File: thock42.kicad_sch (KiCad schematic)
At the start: 45 parts, among them J1 OLED-128x32, SW1 SW_PUSH, SW10 SW_PUSH, SW11 SW_PUSH, SW12 SW_PUSH, SW13 SW_PUSH, SW14 SW_PUSH, SW15 SW_PUSH, SW16 SW_PUSH, SW17 SW_PUSH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

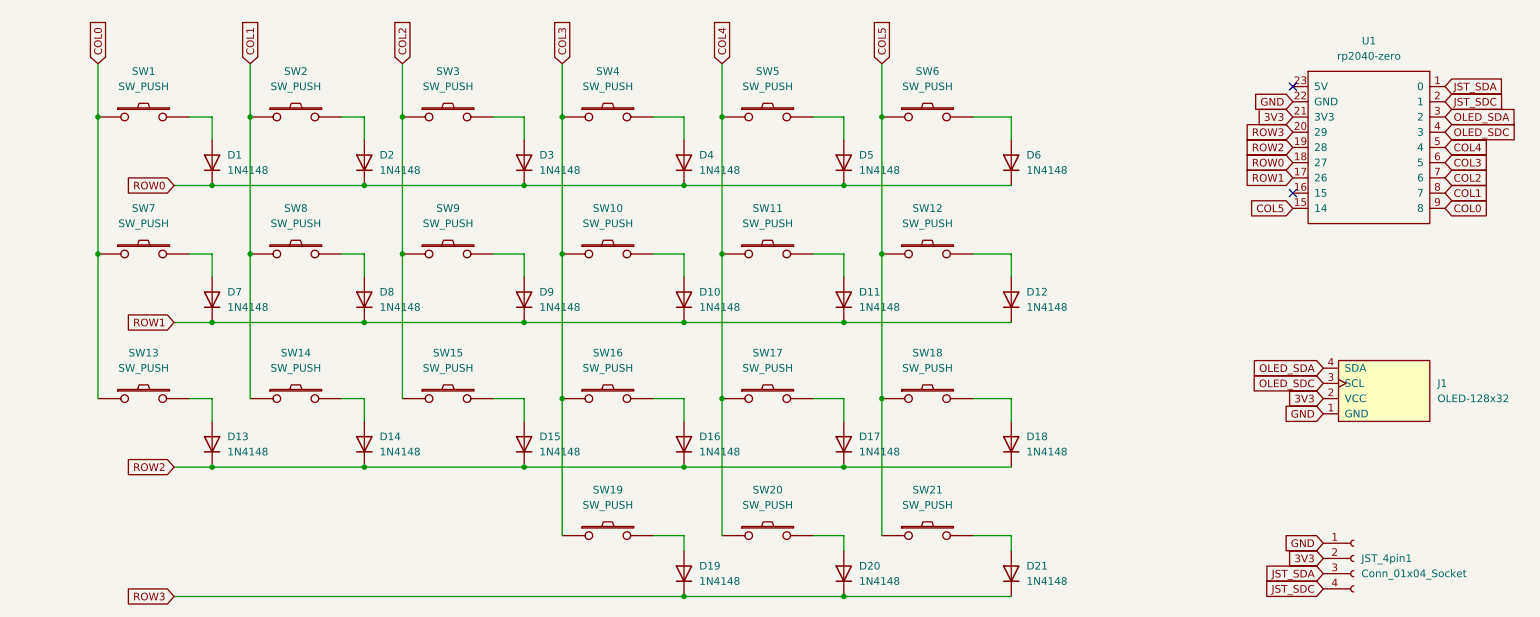
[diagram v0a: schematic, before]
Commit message: 4pin jst with i2c changed to 3pin jst with serial
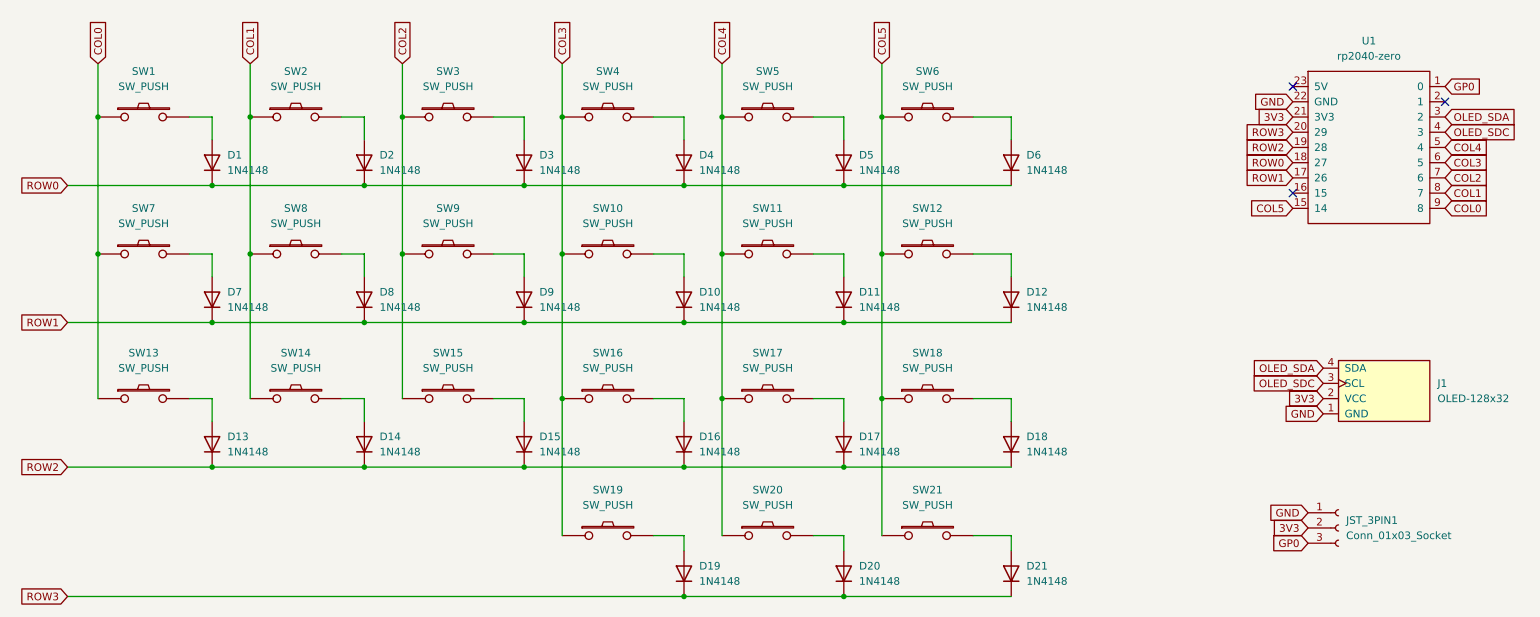
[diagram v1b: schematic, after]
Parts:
- removed JST_4pin1: Conn_01x04_Socket, Connector_JST:JST_XH_S4B-XH-A_1x04_P2.50mm_Horizontal, symbol Connector:Conn_01x04_Socket
- added JST_3PIN1: Conn_01x03_Socket, Connector_JST:JST_XH_S3B-XH-A_1x03_P2.50mm_Horizontal, symbol Connector:Conn_01x03_Socket
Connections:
- net 3V3: now also JST_3PIN1.2 (Pin_2)
- net GND: now also JST_3PIN1.1 (Pin_1)
- net JST_SDA renamed GP0
- net GP0: now also JST_3PIN1.3 (Pin_3)
- net JST_SDC: no longer names the net of U1.2 (1)
- no-connect marks 2 -> 3

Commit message: feat: add switch id silkscreen
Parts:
- SW1, SW10, SW11, SW12, SW13, SW14, SW15, SW16, SW17, SW18, SW19, SW2, SW20, SW21, SW3, SW4, SW5, SW6, SW7, SW8, SW9: footprint pg1350:pg1350-RH -> pg1350:pg1350-RH_silkscreen
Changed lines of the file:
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@@
 			)
 		)
-		(property "Footprint" "pg1350:pg1350-RH"
+		(property "Footprint" "pg1350:pg1350-RH_silkscreen"
 			(at 144.78 58.42 0)
 			(effects
@@
 			)
 		)
-		(property "Footprint" "pg1350:pg1350-RH"
+		(property "Footprint" "pg1350:pg1350-RH_silkscreen"
 			(at 66.04 81.28 0)
 			(effects
@@
 			)
 		)
-		(property "Footprint" "pg1350:pg1350-RH"
+		(property "Footprint" "pg1350:pg1350-RH_silkscreen"
 			(at 118.11 81.28 0)
 			(effects
@@
 			)
 		)
-		(property "Footprint" "pg1350:pg1350-RH"
+		(property "Footprint" "pg1350:pg1350-RH_silkscreen"
 			(at 171.45 81.28 0)
 			(effects
@@
 			)
 		)
-		(property "Footprint" "pg1350:pg1350-RH"
+		(property "Footprint" "pg1350:pg1350-RH_silkscreen"
 			(at 171.45 105.41 0)
 			(effects
@@
 			)
 		)
-		(property "Footprint" "pg1350:pg1350-RH"
+		(property "Footprint" "pg1350:pg1350-RH_silkscreen"
 			(at 118.11 105.41 0)
 			(effects
@@
 			)
 		)
-		(property "Footprint" "pg1350:pg1350-RH"
+		(property "Footprint" "pg1350:pg1350-RH_silkscreen"
 			(at 118.11 58.42 0)
 			(effects
@@
 			)
 		)
-		(property "Footprint" "pg1350:pg1350-RH"
+		(property "Footprint" "pg1350:pg1350-RH_silkscreen"
 			(at 171.45 128.27 0)
 			(effects
@@
 			)
 		)
-		(property "Footprint" "pg1350:pg1350-RH"
+		(property "Footprint" "pg1350:pg1350-RH_silkscreen"
 			(at 144.78 81.28 0)
 			(effects
@@
 			)
 		)
-		(property "Footprint" "pg1350:pg1350-RH"
+		(property "Footprint" "pg1350:pg1350-RH_silkscreen"
 			(at 118.11 128.27 0)
 			(effects
@@
 			)
 		)
-		(property "Footprint" "pg1350:pg1350-RH"
+		(property "Footprint" "pg1350:pg1350-RH_silkscreen"
 			(at 144.78 128.27 0)
 			(effects
@@
 			)
 		)
-		(property "Footprint" "pg1350:pg1350-RH"
+		(property "Footprint" "pg1350:pg1350-RH_silkscreen"
 			(at 91.44 58.42 0)
 			(effects
@@
 			)
 		)
-		(property "Footprint" "pg1350:pg1350-RH"
+		(property "Footprint" "pg1350:pg1350-RH_silkscreen"
 			(at 91.44 105.41 0)
 			(effects
@@
 			)
 		)
-		(property "Footprint" "pg1350:pg1350-RH"
+		(property "Footprint" "pg1350:pg1350-RH_silkscreen"
 			(at 40.64 105.41 0)
 			(effects
@@
 			)
 		)
-		(property "Footprint" "pg1350:pg1350-RH"
+		(property "Footprint" "pg1350:pg1350-RH_silkscreen"
 			(at 66.04 58.42 0)
 			(effects
@@
 			)
 		)
-		(property "Footprint" "pg1350:pg1350-RH"
+		(property "Footprint" "pg1350:pg1350-RH_silkscreen"
 			(at 66.04 105.41 0)
 			(effects
@@
 			)
 		)
-		(property "Footprint" "pg1350:pg1350-RH"
+		(property "Footprint" "pg1350:pg1350-RH_silkscreen"
 			(at 171.45 58.42 0)
 			(effects
@@
 			)
 		)
-		(property "Footprint" "pg1350:pg1350-RH"
+		(property "Footprint" "pg1350:pg1350-RH_silkscreen"
 			(at 91.44 81.28 0)
 			(effects
@@
 			)
 		)
-		(property "Footprint" "pg1350:pg1350-RH"
+		(property "Footprint" "pg1350:pg1350-RH_silkscreen"
 			(at 40.64 58.42 0)
 			(effects
@@
 			)
 		)
-		(property "Footprint" "pg1350:pg1350-RH"
+		(property "Footprint" "pg1350:pg1350-RH_silkscreen"
 			(at 144.78 105.41 0)
 			(effects
@@
 			)
 		)
-		(property "Footprint" "pg1350:pg1350-RH"
+		(property "Footprint" "pg1350:pg1350-RH_silkscreen"
 			(at 40.64 81.28 0)
 			(effects

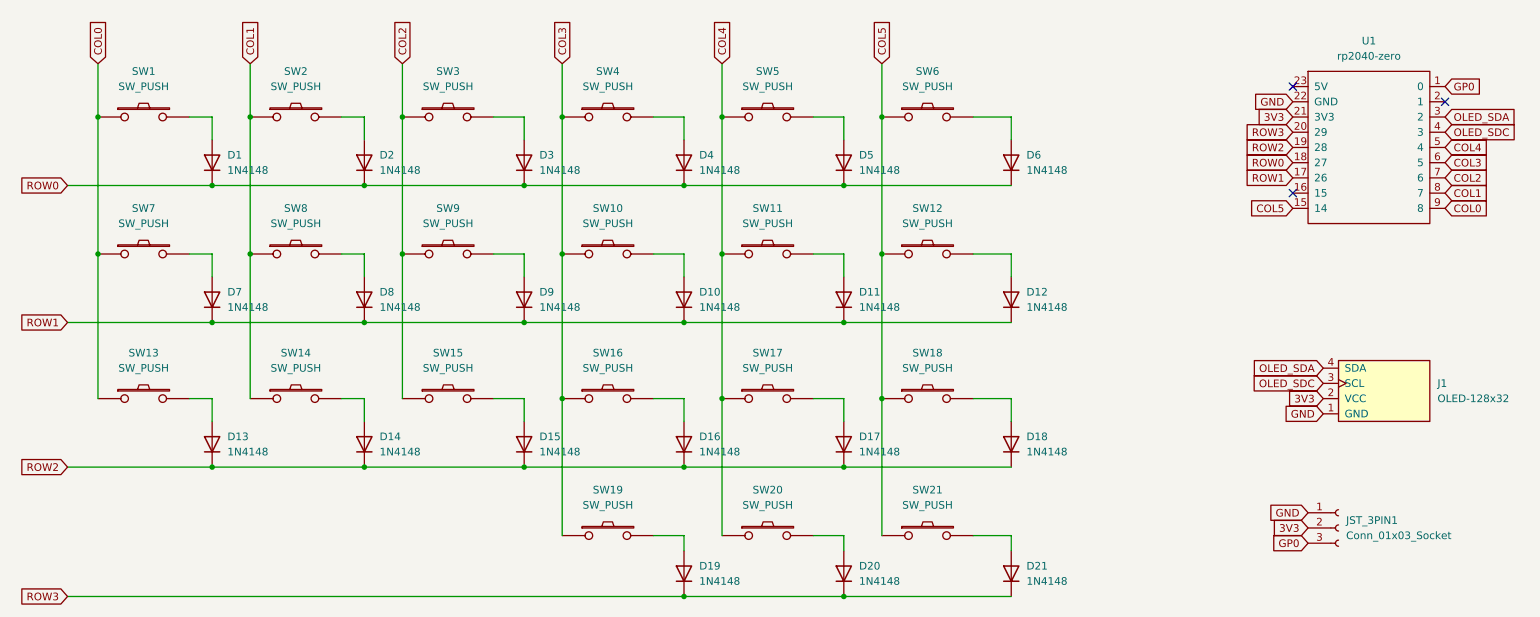
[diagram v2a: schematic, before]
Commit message: update links to libs, jst footprint, and add add mounting hole
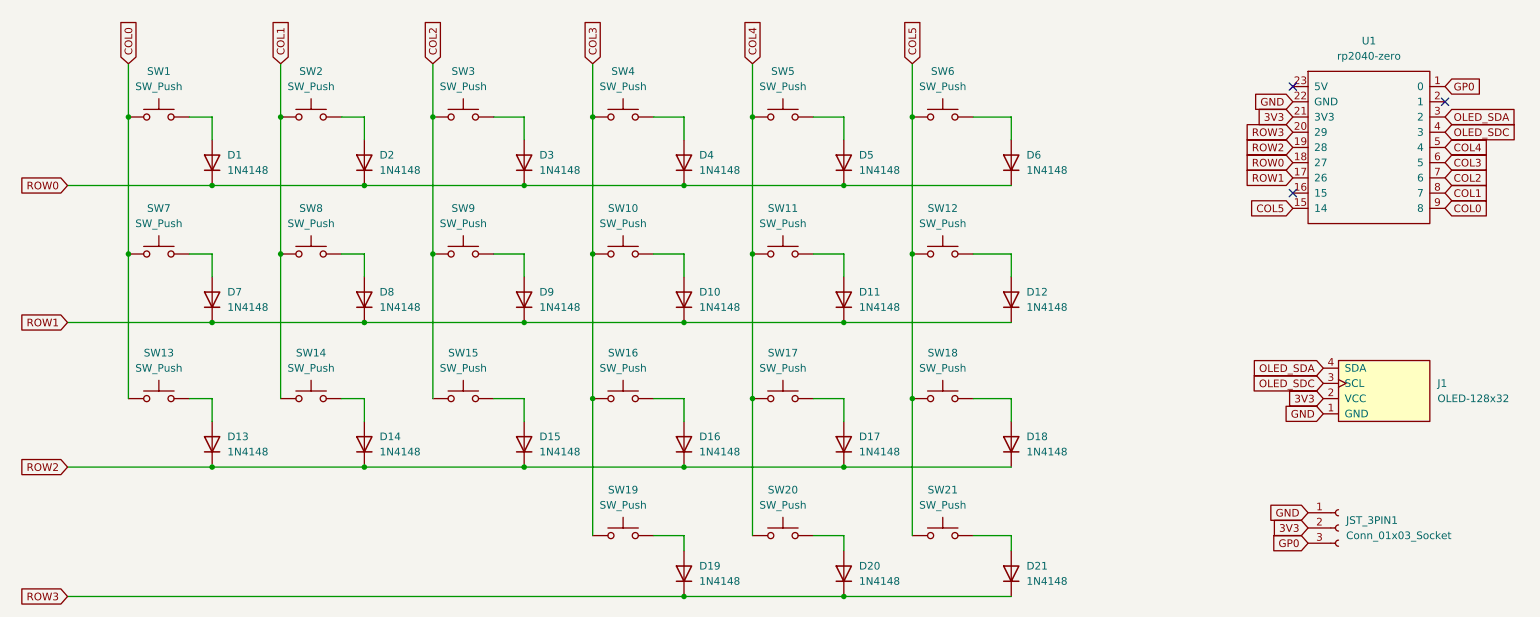
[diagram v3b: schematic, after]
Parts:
- removed SW1, SW10, SW11, SW12, SW13, SW14, SW15, SW16, SW17, SW18, SW19, SW2, SW20, SW21, SW3, SW4, SW5, SW6, SW7, SW8, SW9: SW_PUSH, pg1350:pg1350-RH_silkscreen, symbol kbd:SW_PUSH
- added SW1, SW10, SW11, SW12, SW13, SW14, SW15, SW16, SW17, SW18, SW19, SW2, SW20, SW21, SW3, SW4, SW5, SW6, SW7, SW8, SW9: SW_Push, thock42:pg1350-RH_silkscreen, symbol Switch:SW_Push
- J1: footprint display_kleeb:OLED-128x32-double-sided -> thock42:OLED-128x32-double-sided; symbol display_kleeb:OLED-128x32 -> thock42:OLED-128x32
- JST_3PIN1: footprint Connector_JST:JST_XH_S3B-XH-A_1x03_P2.50mm_Horizontal -> Connector_JST:JST_PH_S3B-PH-K_1x03_P2.00mm_Horizontal
- U1: footprint mcu_kleeb:rp2040-zero-tht_nobtm_reversible -> thock42:rp2040-zero-tht_nobtm_reversible; symbol mcu_kleeb:rp2040-zero -> thock42:rp2040-zero_nobtm
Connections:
- net COL0: now also SW1.1, SW13.1, SW7.1
- net COL1: now also SW14.1, SW2.1, SW8.1
- net COL2: now also SW15.1, SW3.1, SW9.1
- net COL3: now also SW10.1, SW16.1, SW19.1, SW4.1
- net COL4: now also SW11.1, SW17.1, SW20.1, SW5.1
- net COL5: now also SW12.1, SW18.1, SW21.1, SW6.1
- net at D5.2 (A): now also SW5.2
- net at D17.2 (A): now also SW17.2
- net at D8.2 (A): now also SW8.2
- net at D10.2 (A): now also SW10.2
- net at D12.2 (A): now also SW12.2
- net at D11.2 (A): now also SW11.2
- net at D2.2 (A): now also SW2.2
- net at D4.2 (A): now also SW4.2
- net at D18.2 (A): now also SW18.2
- net at D16.2 (A): now also SW16.2
- net at D21.2 (A): now also SW21.2
- net at D1.2 (A): now also SW1.2
- net at D19.2 (A): now also SW19.2
- net at D14.2 (A): now also SW14.2
- net at D20.2 (A): now also SW20.2
- net at D9.2 (A): now also SW9.2
- net at D3.2 (A): now also SW3.2
- net at D15.2 (A): now also SW15.2
- net at D13.2 (A): now also SW13.2
- net at D7.2 (A): now also SW7.2
- net at D6.2 (A): now also SW6.2

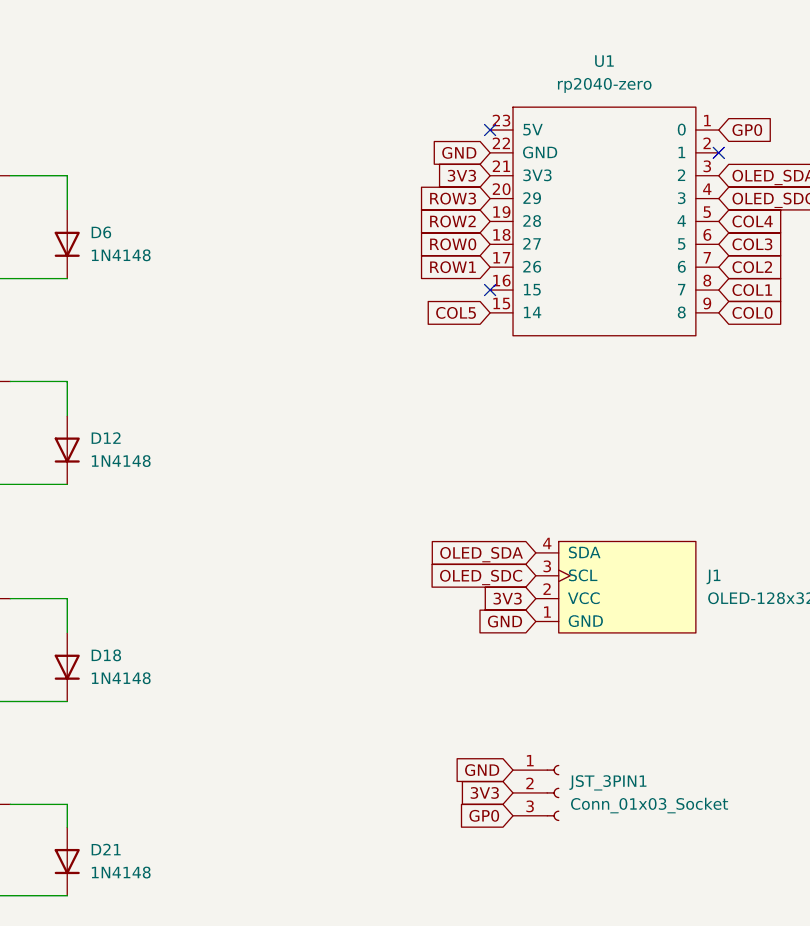
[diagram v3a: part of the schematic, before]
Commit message: add i2c pullups and redesign thumb cluster
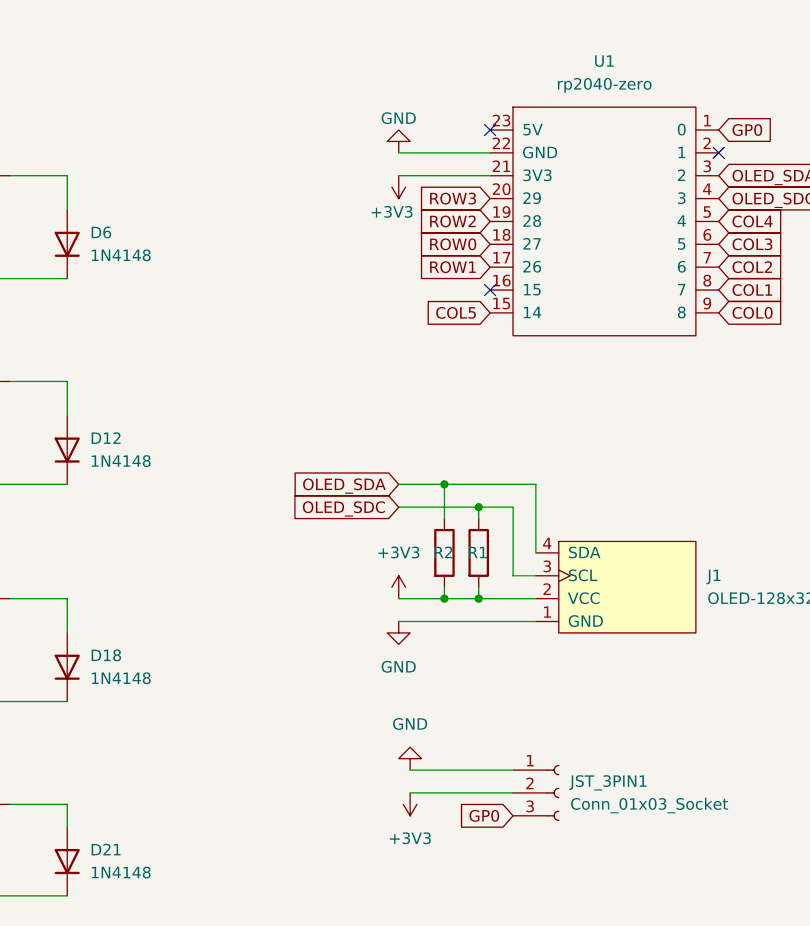
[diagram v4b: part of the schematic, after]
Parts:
- added R1, R2: R, Resistor_THT:R_Axial_DIN0207_L6.3mm_D2.5mm_P10.16mm_Horizontal, symbol Device:R
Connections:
- net OLED_SDA: now also R2.1
- net OLED_SDC: now also R1.1
- net 3V3 renamed +3V3
- net +3V3: now also R1.2, R2.2
